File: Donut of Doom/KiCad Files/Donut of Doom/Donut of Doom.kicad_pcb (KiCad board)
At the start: 2 copper layers, 25 x 53 mm, 35 parts, among them Q1 Q_NMOS_GSD, U3 H3LIS331DLTR

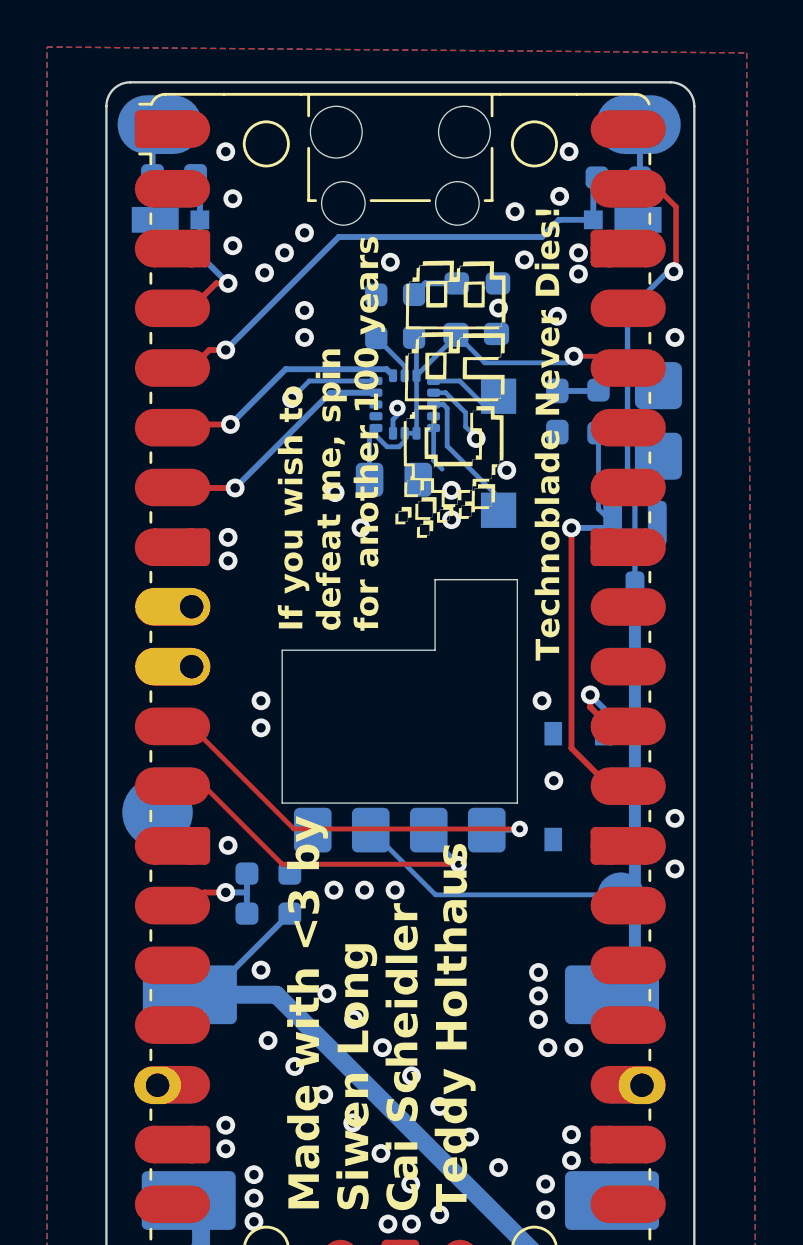
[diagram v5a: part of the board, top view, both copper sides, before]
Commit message: Added more breakouts, corrected MOSFET, better esc and led pads.
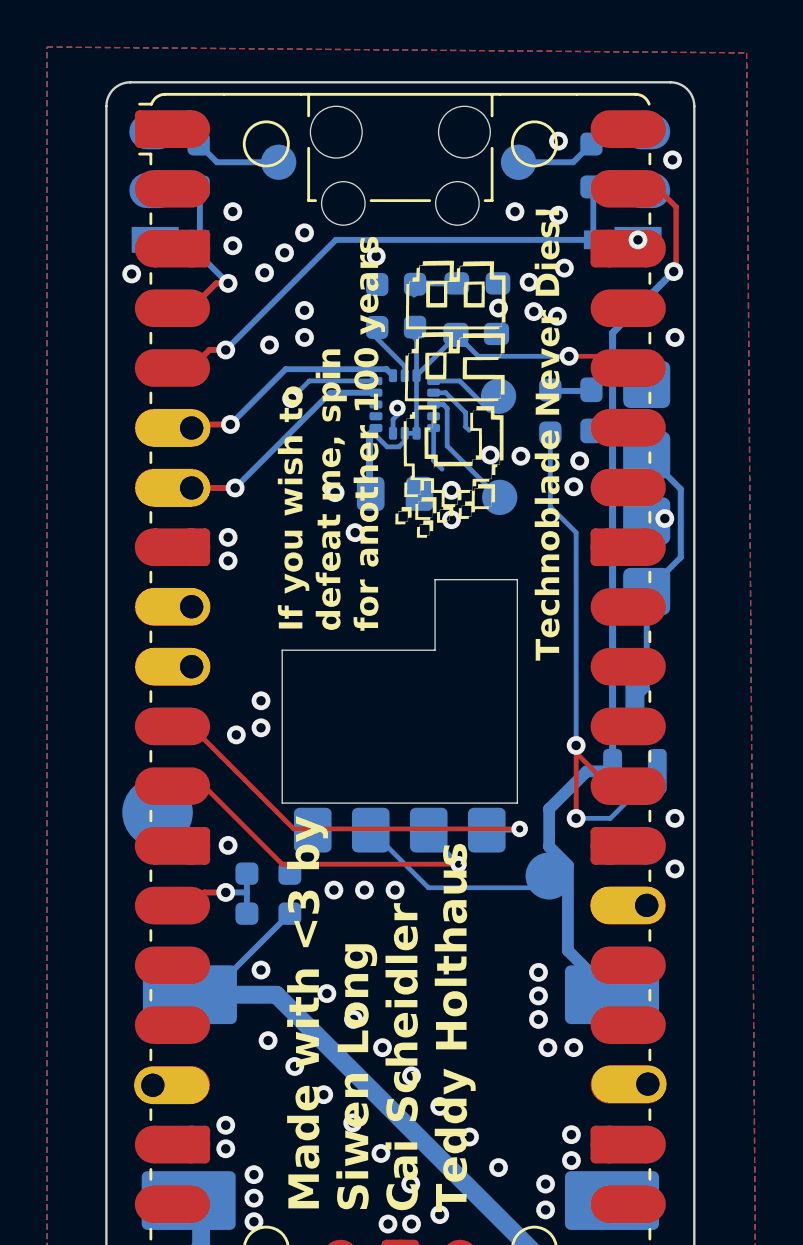
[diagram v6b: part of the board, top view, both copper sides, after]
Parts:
- removed ? (x4): , 
- removed PWM1, PWM2: ~, Battlebots:Oval Pad
- removed S1: TL3365AF180QG, TL3365AF180QG:SW_TL3365AF180QG
- added D6: 5V LED Strip, Battlebots:2 pth Pads, B.Cu at (161.1, 88.7)
- added ESC1: ~, Battlebots:2_2mmx1.5mm_smd_pad, B.Cu at (140.1, 71.9)
- added ESC2: ~, Battlebots:2_2mmx1.5mm_smd_pad, B.Cu at (161.1, 71.9)
- added EX1: GPIO6, Battlebots:Pico_pth_pad, B.Cu at (141.8, 90.8)
- added EX2: GPIO7, Battlebots:Pico_pth_pad, F.Cu at (141.8, 93.4)
- added EX3: GP13, Battlebots:Pico_pth_pad, F.Cu at (140.1, 111.2)
- added EX4: GP18, Battlebots:Pico_pth_pad, F.Cu at (161.2, 111.2)
- added EX5: GPIO4, Battlebots:Pico_pth_pad, F.Cu at (141.8, 83.2)
- added EX6: GPIO5, Battlebots:Pico_pth_pad, F.Cu at (141.8, 85.8)
- added EX7: GPIO21, Battlebots:Pico_pth_pad, F.Cu at (161.1, 103.5)
- added TP7: ESC1, TestPoint:TestPoint_Pad_D1.5mm, B.Cu at (145.4, 72.0)
- added TP8: ESC2, TestPoint:TestPoint_Pad_D1.5mm, B.Cu at (155.7, 72.0)
- D1: value RED 2V LED -> 5V LED Strip
- TP1, TP2: footprint TestPoint:TestPoint_Pad_1.5x1.5mm -> TestPoint:TestPoint_Pad_D1.5mm
- moved Q1 7.55 mm to (160.6, 96.3), turned to 90 degrees
- moved TP3 3.17 mm to (156.9, 102.3)
- moved G*** 2.84 mm to (145.3, 88.6), turned to 180 degrees
- moved R1 2.05 mm to (157.0, 82.5)
- moved D2 1.45 mm to (158.8, 82.5)
- moved R3 1.26 mm to (158.8, 72.1), turned to 90 degrees
- moved R2 1.13 mm to (142.1, 72.1), turned to 90 degrees
- moved D3 0.85 mm to (141.1, 75.2)
- moved D4 0.85 mm to (159.8, 75.2)
- moved C1 0.60 mm to (150.4, 86.0)
- moved TP1 0.55 mm to (154.8, 86.2)
- moved G*** 0.55 mm to (143.0, 79.2), turned to 0 degrees
- moved D1 0.50 mm to (161.1, 82.9)
- moved R4 0.44 mm to (149.6, 78.1)
- moved R5 0.44 mm to (151.2, 78.0)
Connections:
- A1 pad 10: unconnected-(A1-GPIO7-Pad10) -> Net-(A1-GPIO7)
- A1 pad 17: unconnected-(A1-GPIO13-Pad17) -> Net-(A1-GPIO13)
- A1 pad 24: unconnected-(A1-GPIO18-Pad24) -> Net-(A1-GPIO18)
- A1 pad 27: unconnected-(A1-GPIO21-Pad27) -> Net-(A1-GPIO21)
- A1 pad 30: Net-(A1-RUN) -> unconnected-(A1-RUN-Pad30)
- A1 pad 9: unconnected-(A1-GPIO6-Pad9) -> Net-(A1-GPIO6)
- Q1 pad 2: Net-(D1-A) -> +5V
- Q1 pad 3: +5V -> Net-(D1-A)
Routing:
- net Net-(D1-A): track 2.87 -> 11.9 mm
- net /Directional LED: track 17.6 -> 23.4 mm, vias 1 -> 2
- net Net-(ESC2-Signal): track 2.62 -> 6.43 mm
- net Net-(A1-RUN): track 3.57 -> 0.00 mm, vias 1 -> 0
- net Net-(ESC1-Signal): track 2.53 -> 5.99 mm
- net /ESC1: track 7.18 -> 6.62 mm
- net GND: vias 69 -> 74
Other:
- board text added: "Donut of Doom PCB V1"
- board text added: "Z"
- board text removed: "P10"
- board text removed: "P17"
- board text removed: "P24"
- board text removed: "P9"
- board text removed: "PCB V1 Donut of Doom"
- board text removed: "Reset>"

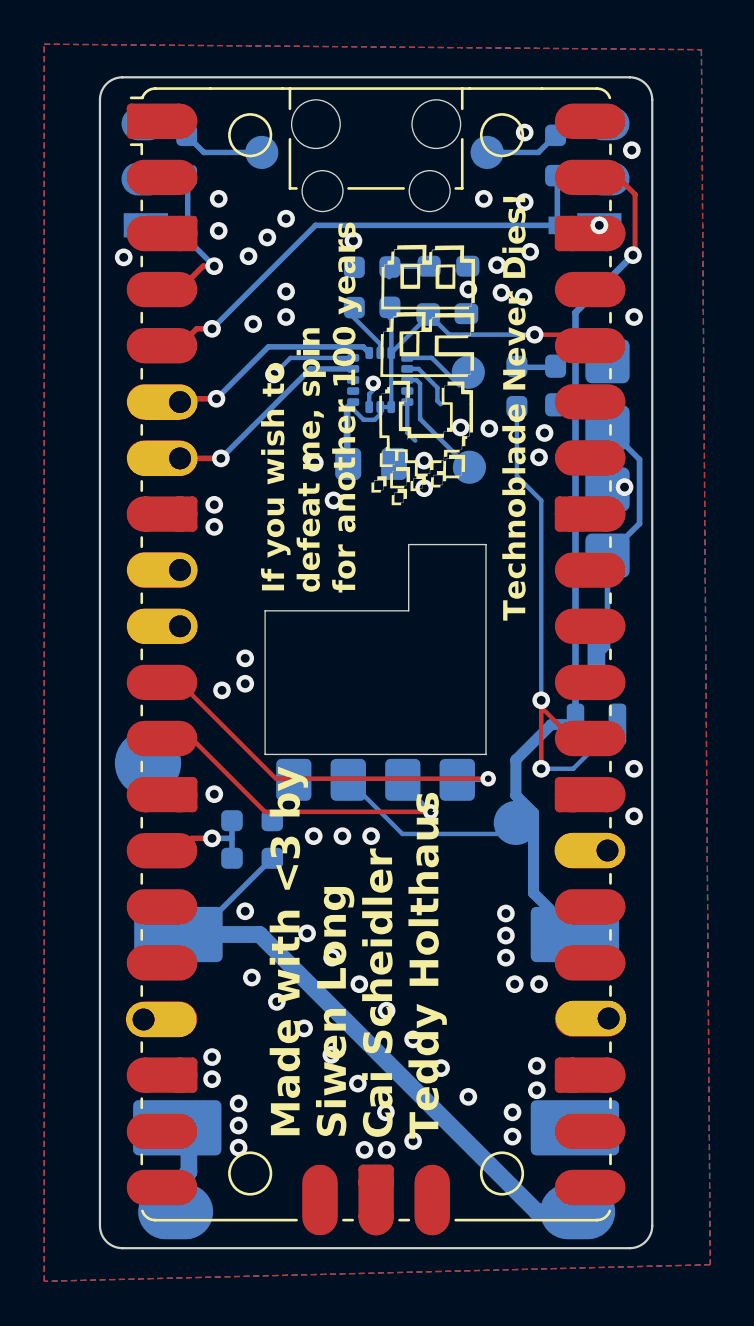
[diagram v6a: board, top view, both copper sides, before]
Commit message: Added better GND connections and Labels
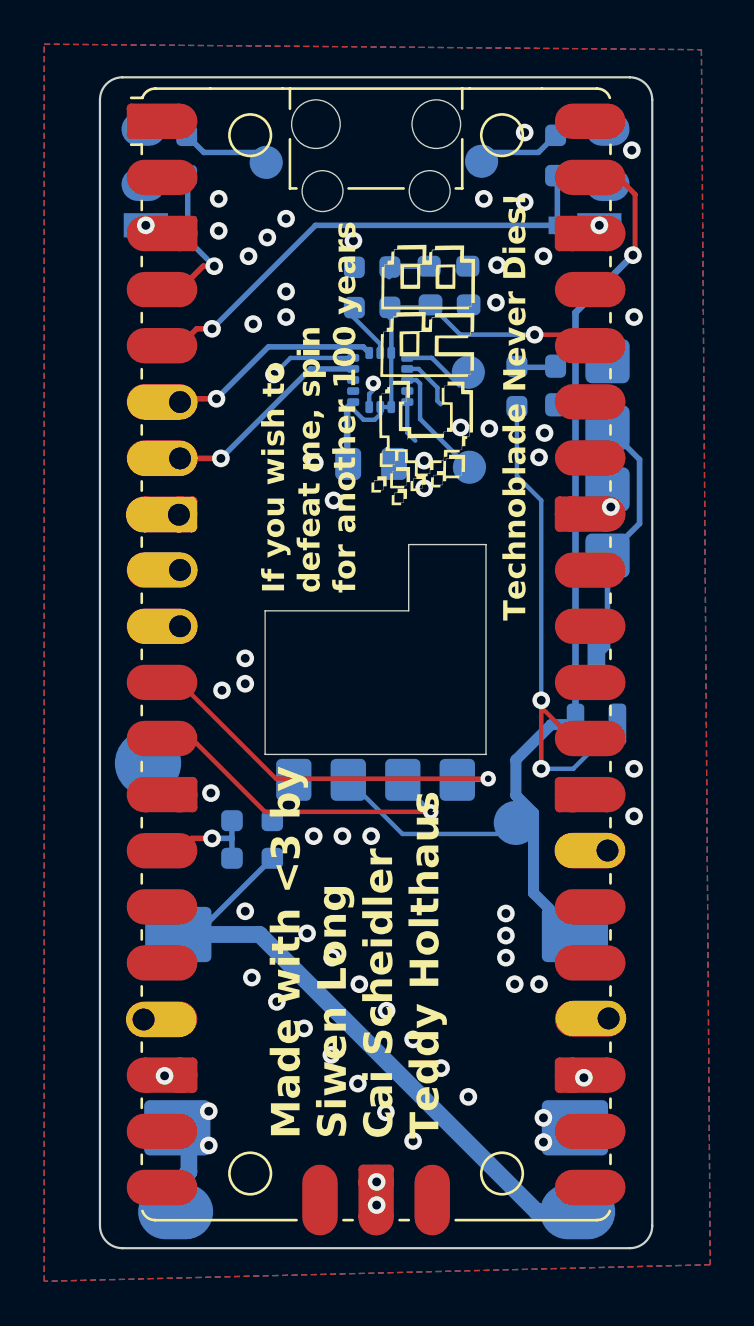
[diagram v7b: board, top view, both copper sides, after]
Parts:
- removed the G*** at (145.3, 88.6)
- added EX8: GND, Battlebots:Pico_pth_GND, F.Cu at (141.7, 88.3)
- added G***: LOGO, LOGO, B.Cu at (146.3, 88.3)
- added G***: LOGO, LOGO, B.Cu at (140.1, 69.5)
- added G***: LOGO, LOGO, B.Cu at (161.1, 69.5)
- moved TP7 0.49 mm to (145.7, 72.4)
- moved TP8 0.47 mm to (155.4, 72.3)
- moved C2 0.41 mm to (153.9, 78.8)
- moved ESC1 0.25 mm to (140.1, 72.2)
- moved ESC2 0.25 mm to (161.1, 72.2)
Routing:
- net GND: vias 74 -> 67

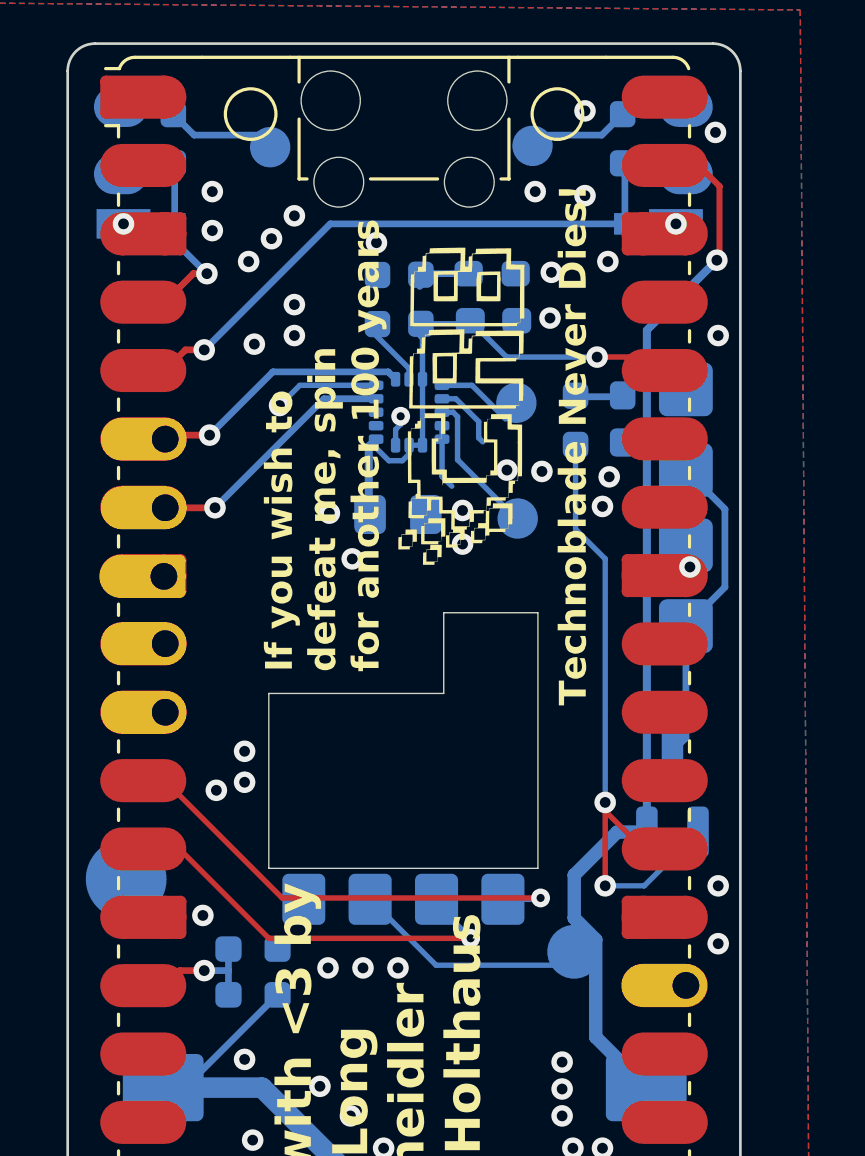
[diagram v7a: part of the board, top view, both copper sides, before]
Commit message: Turned accelorometer 45 degrees, increased clearence on elrs reciever
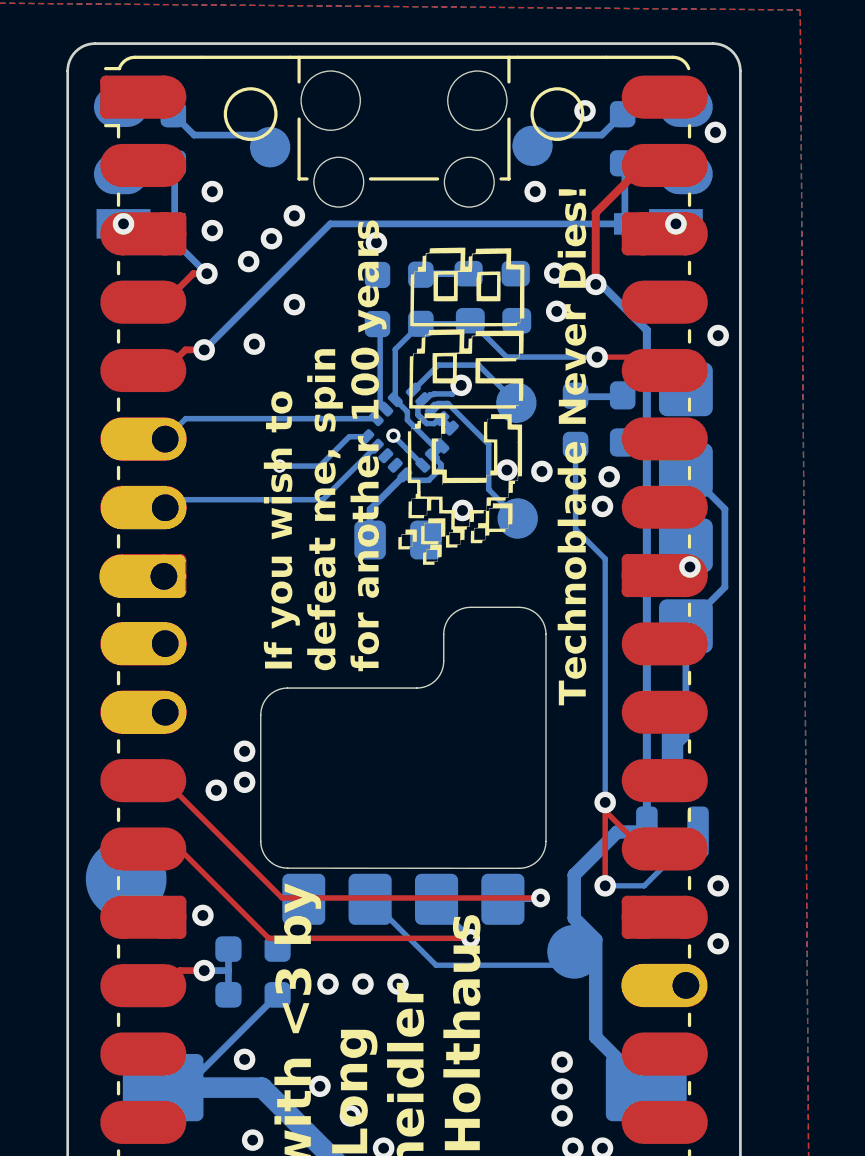
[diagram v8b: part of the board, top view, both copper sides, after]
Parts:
- moved C1 0.95 mm to (150.4, 87.0)
- moved U3 0.75 mm to (150.8, 83.0), turned to 45 degrees
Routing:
- net +3V3: track 18.2 -> 20.6 mm
- net Net-(U3-INT2): track 2.88 -> 4.79 mm
- net +5V: track 50.4 -> 48.6 mm
- net /I2C0 SDA: track 9.72 -> 8.16 mm, vias 1 -> 0
- net Net-(U3-SDO/SA0): track 2.11 -> 3.35 mm
- net /I2C0 SCL: track 9.62 -> 8.79 mm, vias 1 -> 0
- net Net-(D5-A): track 2.01 -> 1.34 mm
- net GND: vias 67 -> 62
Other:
- board text added: "G"
- board text removed: "BATT-> SENSE"
